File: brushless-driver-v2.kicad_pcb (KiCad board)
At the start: 2 copper layers, 86.5 x 63 mm, 52 parts, among them J1 Conn_01x07_Socket, J2 encoder, J3 motor, U1 TCMT1100, U2 TCMT1100, U3 TCMT1100, U5 L7805

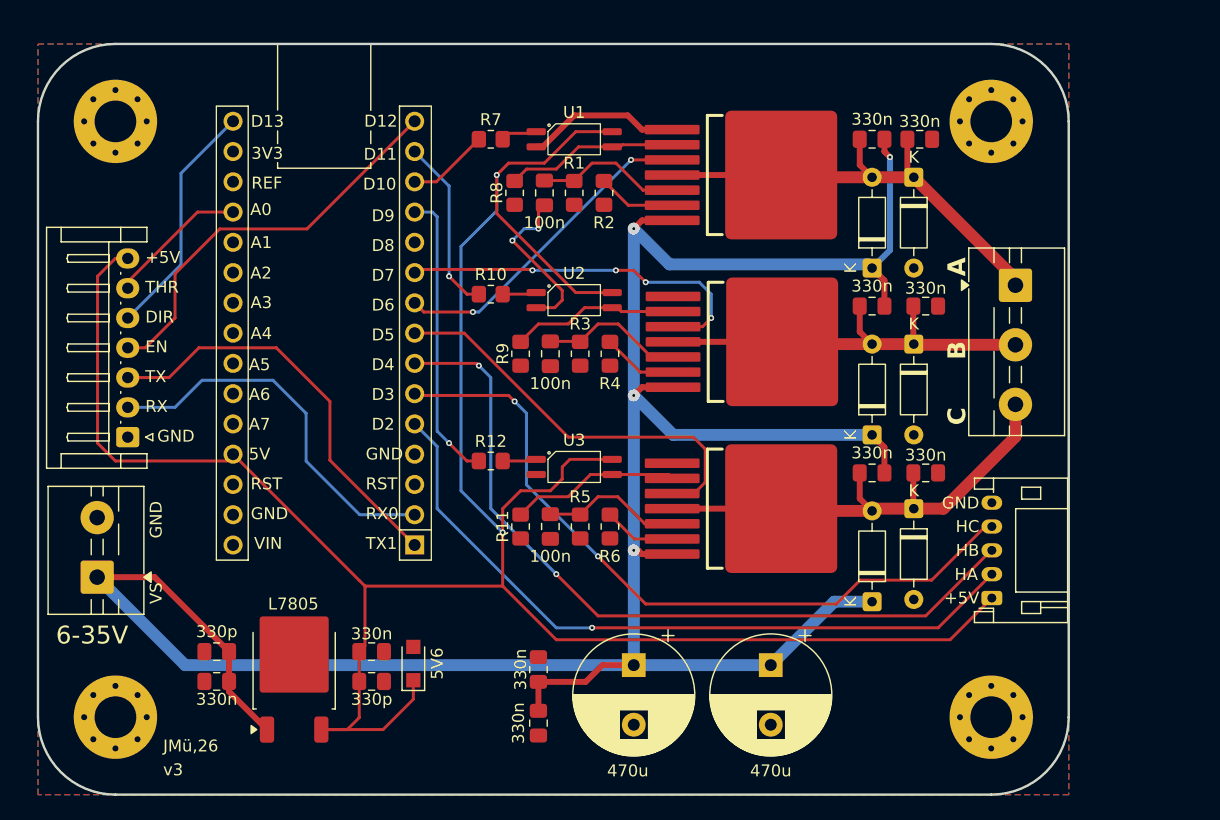
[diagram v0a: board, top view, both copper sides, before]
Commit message: Updated Footprint of JST connector to 2mm pitch
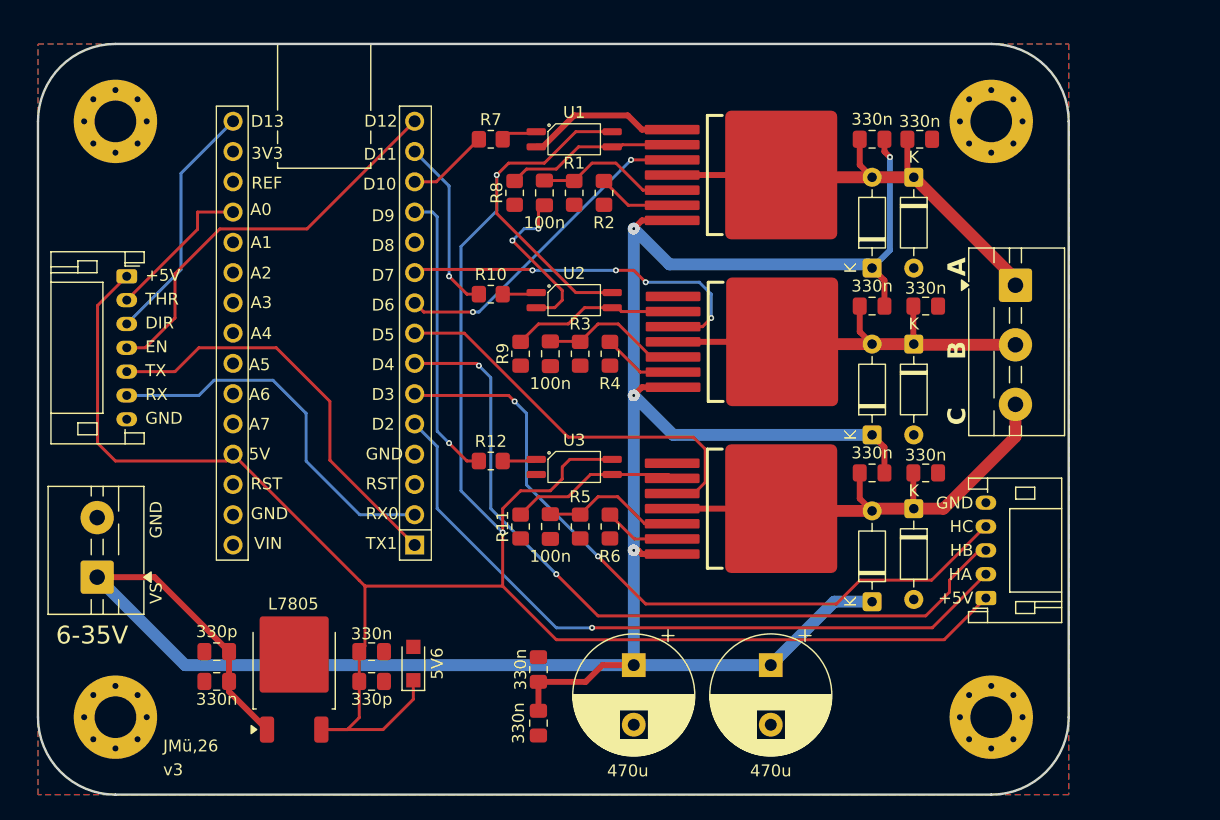
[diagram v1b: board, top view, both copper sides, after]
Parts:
- J1: footprint Connector_JST:JST_EH_S7B-EH_1x07_P2.50mm_Horizontal -> Connector_JST:JST_PH_S7B-PH-K_1x07_P2.00mm_Horizontal
- moved J1 13.5 mm to (111.0, 103.0), turned to -90 degrees
- moved J2 0.50 mm to (183.1, 130.0)
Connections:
- J1 pad 1: GND -> +5V
- J1 pad 2: RX -> THR
- J1 pad 3: TX -> DIR
- J1 pad 5: DIR -> TX
- J1 pad 6: THR -> RX
- J1 pad 7: +5V -> GND
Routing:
- net +5V: track 203.7 -> 201.1 mm
- net THR: track 11.8 -> 12.8 mm
- net HC: track 62.0 -> 61.4 mm
- net DIR: track 20.2 -> 20.7 mm
- net HA: track 60.4 -> 59.9 mm

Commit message: Improvements, more to be done
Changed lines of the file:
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@@
 		)
 		(fp_text user "K"
-			(at -1.5 0 180)
+			(at -1.5 0 0)
 			(layer "F.SilkS")
 			(effects
@@
 			(at 0 -1.68 90)
 			(layer "F.SilkS")
-			(hide yes)
 			(effects
 				(font
@@
 			(at 7.367677 -4 0)
 			(layer "F.SilkS")
-			(hide yes)
 			(effects
 				(font
@@
 			(at 0 -1.68 0)
 			(layer "F.SilkS")
-			(hide yes)
 			(effects
 				(font
@@
 			(at 0 -1.68 0)
 			(layer "F.SilkS")
-			(hide yes)
 			(effects
 				(font
@@
 			(at 0 -3.575 90)
 			(layer "F.SilkS")
-			(hide yes)
 			(effects
 				(font
@@
 			(at 0 -4.45 0)
 			(layer "F.SilkS")
-			(hide yes)
 			(effects
 				(font
@@
 			(at 3.81 -2.12 90)
 			(layer "F.SilkS")
-			(hide yes)
 			(effects
 				(font
@@
 			(at 0 -1.68 0)
 			(layer "F.SilkS")
-			(hide yes)
 			(effects
 				(font
@@
 			(at 0 -1.68 0)
 			(layer "F.SilkS")
-			(hide yes)
 			(effects
 				(font
@@
 		)
 		(fp_text user "K"
-			(at -1.69 0 180)
+			(at -1.69 0 0)
 			(layer "F.SilkS")
 			(effects
@@
 			(at 0 -1.68 0)
 			(layer "F.SilkS")
-			(hide yes)
 			(effects
 				(font
@@
 			(at 0 -4.45 0)
 			(layer "F.SilkS")
-			(hide yes)
 			(effects
 				(font
@@
 			(at 6 -2.55 90)
 			(layer "F.SilkS")
-			(hide yes)
 			(effects
 				(font
@@
 			(at 0 -1.68 0)
 			(layer "F.SilkS")
-			(hide yes)
 			(effects
 				(font
@@
 			(at 0 -1.68 0)
 			(layer "F.SilkS")
-			(hide yes)
 			(effects
 				(font
@@
 			(at 0 -3.5 90)
 			(layer "F.SilkS")
-			(hide yes)
 			(effects
 				(font
@@
 			(at 2.25 -5.12 90)
 			(layer "F.SilkS")
-			(hide yes)
 			(effects
 				(font
@@
 			(at 0 -1.68 90)
 			(layer "F.SilkS")
-			(hide yes)
 			(effects
 				(font
@@
 		)
 		(fp_text user "K"
-			(at -1.69 0 180)
+			(at -1.69 0 0)
 			(layer "F.SilkS")
 			(effects
@@
 			(at 0 -1.68 90)
 			(layer "F.SilkS")
-			(hide yes)
 			(effects
 				(font
@@
 			(at 0 -4.45 0)
 			(layer "F.SilkS")
-			(hide yes)
 			(effects
 				(font
@@
 			(at 0 -4.5 90)
 			(layer "F.SilkS")
-			(hide yes)
 			(effects
 				(font
@@
 			(at 7.367677 -5.5 0)
 			(layer "F.SilkS")
-			(hide yes)
 			(effects
 				(font
@@
 			(at 7.62 -5.08 180)
 			(layer "F.SilkS")
-			(hide yes)
 			(effects
 				(font
@@
 			(at 0 -2 90)
 			(layer "F.SilkS")
-			(hide yes)
 			(effects
 				(font
@@
 			(at 0 -1.68 0)
 			(layer "F.SilkS")
-			(hide yes)
 			(effects
 				(font
@@
 			(at 0 -3.5 90)
 			(layer "F.SilkS")
-			(hide yes)
 			(effects
 				(font
@@
 			(at 0 -1.68 90)
 			(layer "F.SilkS")
-			(hide yes)
 			(effects
 				(font
@@
 		(tags "THT terminal block MaiXu MX126-5.0-03P pitch 5mm size 15.5x7.8mm drill 1.3mm pad 2.8mm")
 		(property "Reference" "J3"
-			(at 4.75 -5.12 270)
+			(at 4.75 -5.12 90)
 			(layer "F.SilkS")
 			(hide yes)
@@
 		)
 		(property "Value" "motor"
-			(at 4.75 4.92 270)
+			(at 4.75 4.92 90)
 			(layer "F.Fab")
 			(hide yes)
@@
 		)
 		(property "Datasheet" "~"
-			(at 0 0 270)
+			(at 0 0 90)
 			(layer "F.Fab")
 			(hide yes)
@@
 		)
 		(property "Description" ""
-			(at 0 0 270)
+			(at 0 0 90)
 			(layer "F.Fab")
 			(hide yes)
@@
 		)
 		(fp_text user "${REFERENCE}"
-			(at 4.75 2.65 270)
+			(at 4.75 2.65 90)
 			(layer "F.Fab")
 			(effects
@@
 			(at 0 -4.45 0)
 			(layer "F.SilkS")
-			(hide yes)
 			(effects
 				(font
@@
 			(at 3.81 -2.12 90)
 			(layer "F.SilkS")
-			(hide yes)
 			(effects
 				(font
@@
 			(at 0 -1.68 90)
 			(layer "F.SilkS")
-			(hide yes)
 			(effects
 				(font
@@
 			(at 0 -1.68 0)
 			(layer "F.SilkS")
-			(hide yes)
 			(effects
 				(font
@@
 			(at 0 -1.68 0)
 			(layer "F.SilkS")
-			(hide yes)
 			(effects
 				(font
@@
 	)
 	(gr_text "+5V"
-		(at 182 130 0)
+		(at 181.5 130 0)
 		(layer "F.SilkS")
 		(effects
@@
 	)
 	(gr_text "A"
-		(at 181.5 103 90)
+		(at 180.5 103 90)
 		(layer "F.SilkS")
 		(effects
@@
 	)
 	(gr_text "GND"
-		(at 114 125 90)
+		(at 116.5 125 90)
 		(layer "F.SilkS")
 		(effects
@@
 	)
 	(gr_text "HC"
-		(at 182 124 0)
+		(at 181.5 124 0)
 		(layer "F.SilkS")
 		(effects
@@
 	)
 	(gr_text "B"
-		(at 181.5 110 90)
+		(at 180.5 110 90)
 		(layer "F.SilkS")
 		(effects
@@
 	)
 	(gr_text "HB"
-		(at 182 126 0)
+		(at 181.5 126 0)
 		(layer "F.SilkS")
 		(effects
@@
 	)
 	(gr_text "VS"
-		(at 114 130.5 90)
+		(at 116.5 130.5 90)
 		(layer "F.SilkS")
 		(effects
@@
 	)
 	(gr_text "GND"
-		(at 182.001112 122.023428 0)
+		(at 181.501112 122.023428 0)
 		(layer "F.SilkS")
 		(effects
@@
 	)
 	(gr_text "C"
-		(at 181.5 115.5 90)
+		(at 180.5 115.5 90)
 		(layer "F.SilkS")
 		(effects
@@
 	)
 	(gr_text "HA"
-		(at 181.887958 128.020615 0)
+		(at 181.387958 128.020615 0)
 		(layer "F.SilkS")
 		(effects

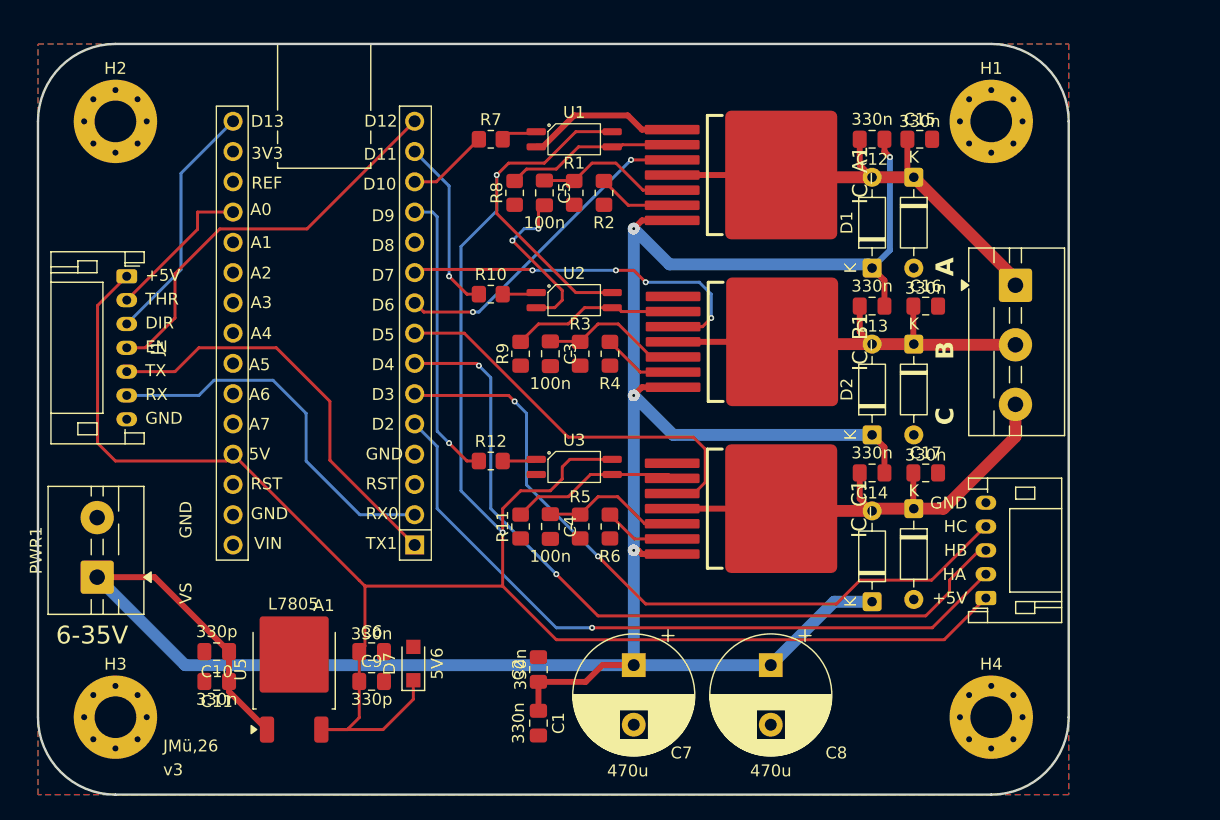
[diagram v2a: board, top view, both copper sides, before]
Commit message: Started on version 3. Major redesign according to dev board for the IFX007T. Previous version was unfit for continous operation - now zones instead of traces for high current lines.
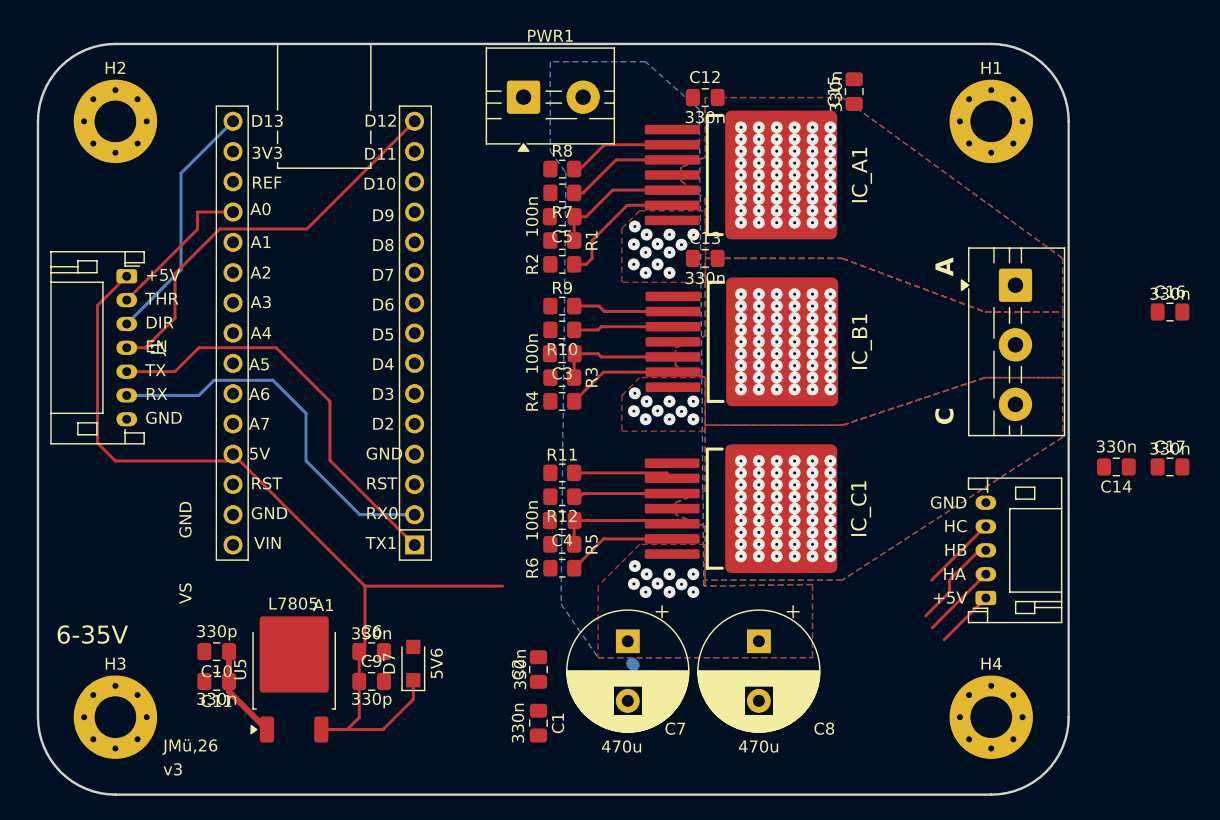
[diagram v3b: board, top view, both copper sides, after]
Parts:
- removed D1, D2, D3, D4, D5, D6: 1N914, Diode_THT:D_DO-35_SOD27_P7.62mm_Horizontal
- removed U1, U2, U3: TCMT1100, meiBib:SOP-4_4.4x2.6mm_P1.27mm
- R10, R12, R7: value 220R -> 10k
- moved PWR1 53.9 mm to (144.2, 88.0), turned to 0 degrees
- moved C14 20.5 mm to (194.0, 119.0)
- moved C16 20.5 mm to (198.5, 106.0)
- moved C17 20.5 mm to (198.5, 119.0)
- moved C13 14.6 mm to (159.5, 101.5), turned to 0 degrees
- moved C12 14.4 mm to (159.5, 88.0), turned to 0 degrees
- moved R7 7.50 mm to (147.5, 96.0), turned to 180 degrees
- moved R2 6.95 mm to (147.5, 102.0), turned to 180 degrees
- moved C15 6.80 mm to (172.0, 87.5), turned to 90 degrees
- moved R10 6.71 mm to (147.5, 107.5), turned to 180 degrees
- moved R12 6.71 mm to (147.5, 121.5), turned to 180 degrees
- moved R11 5.70 mm to (147.5, 119.5), turned to 180 degrees
- moved R4 5.66 mm to (147.5, 113.5), turned to 180 degrees
- moved R6 5.32 mm to (147.5, 127.5), turned to 180 degrees
- moved R9 5.32 mm to (147.5, 105.5), turned to 180 degrees
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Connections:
- net Net-(D1-A) renamed A_OUT
- net Net-(D2-A) renamed B_OUT
- net Net-(D3-A) renamed C_OUT
- IC_A1 pad 3: INH_A -> Net-(IC_A1-INH)
- IC_B1 pad 3: INH_B -> Net-(IC_B1-INH)
- IC_C1 pad 3: INH_C -> Net-(IC_C1-INH)
- PWR1 pad 1: VS -> GND
- PWR1 pad 2: GND -> VS
- R10 pad 1: B -> Net-(IC_B1-INH)
- R10 pad 2: Net-(R10-Pad2) -> INH_B
- R11 pad 2: GND -> C
- R12 pad 1: C -> Net-(IC_C1-INH)
- R12 pad 2: Net-(R12-Pad2) -> INH_C
- R7 pad 1: A -> Net-(IC_A1-INH)
- R7 pad 2: Net-(R7-Pad2) -> INH_A
- R8 pad 2: GND -> A
- R9 pad 2: GND -> B
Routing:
- net VS: track 212.2 -> 8.51 mm, vias 4 -> 33
- net +5V: track 201.1 -> 84.6 mm, vias 2 -> 0
- net HB: track 66.0 -> 7.91 mm, vias 2 -> 0
- net HC: track 61.4 -> 6.58 mm, vias 2 -> 0
- net HA: track 59.9 -> 6.36 mm, vias 1 -> 0
- net C_OUT: track 41.0 -> 0.27 mm, vias 0 -> 54
- net A_OUT: track 40.0 -> 0.80 mm, vias 0 -> 54
- net B_OUT: track 35.7 -> 0.27 mm, vias 0 -> 54
- net INH_C: track 34.4 -> 0.00 mm
- net INH_B: track 31.4 -> 0.38 mm, vias 4 -> 0
- net INH_A: track 27.2 -> 0.00 mm, vias 2 -> 0
- net GND: track 27.0 -> 0.00 mm, vias 2 -> 0
- net C: track 24.6 -> 0.00 mm, vias 1 -> 0
- net B: track 14.8 -> 0.00 mm, vias 1 -> 0
- net Net-(IC_A1-INH): track 0.00 -> 9.37 mm
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- added copper zone on B.Cu, net A_OUT
- added copper zone on F.Cu, net A_OUT
- added copper zone on B.Cu, net B_OUT
- added copper zone on F.Cu, net B_OUT
- added copper zone on B.Cu, net C_OUT
- added copper zone on F.Cu, net C_OUT
- added copper zone on B.Cu, net VS
- added copper zone on F.Cu, net VS
- removed copper zone on B.Cu, net GND
- removed copper zone on F.Cu, net GND
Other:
- board text removed: "B"

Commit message: finished rework
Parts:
- removed C12, C13, C14, C15, C16, C17: 330n, Capacitor_SMD:C_0805_2012Metric_Pad1.18x1.45mm_HandSolder
- R1, R3, R5: value 10k -> 5k6
- moved C1 7.02 mm to (146.0, 133.5), turned to 180 degrees
- moved C2 5.52 mm to (146.0, 130.5), turned to 180 degrees
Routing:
- net HC: track 6.58 -> 80.5 mm, vias 0 -> 1
- net HB: track 7.91 -> 80.6 mm
- net HA: track 6.36 -> 76.7 mm
- net +5V: track 84.6 -> 125.0 mm
- net VS: track 8.51 -> 43.9 mm, vias 33 -> 49
- net C: track 0.00 -> 31.9 mm, vias 0 -> 1
- net INH_C: track 0.00 -> 23.5 mm, vias 0 -> 1
- net B: track 0.00 -> 23.2 mm, vias 0 -> 1
- net INH_A: track 0.00 -> 19.3 mm
- net INH_B: track 0.38 -> 15.5 mm, vias 0 -> 1
- net A: track 0.00 -> 11.8 mm, vias 0 -> 1
- net THR: track 12.8 -> 12.0 mm
- added copper zone on B.Cu, net GND
- added copper zone on F.Cu, net GND
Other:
- board text added: "B"
- board text added: "v4"
- board text removed: "v3"

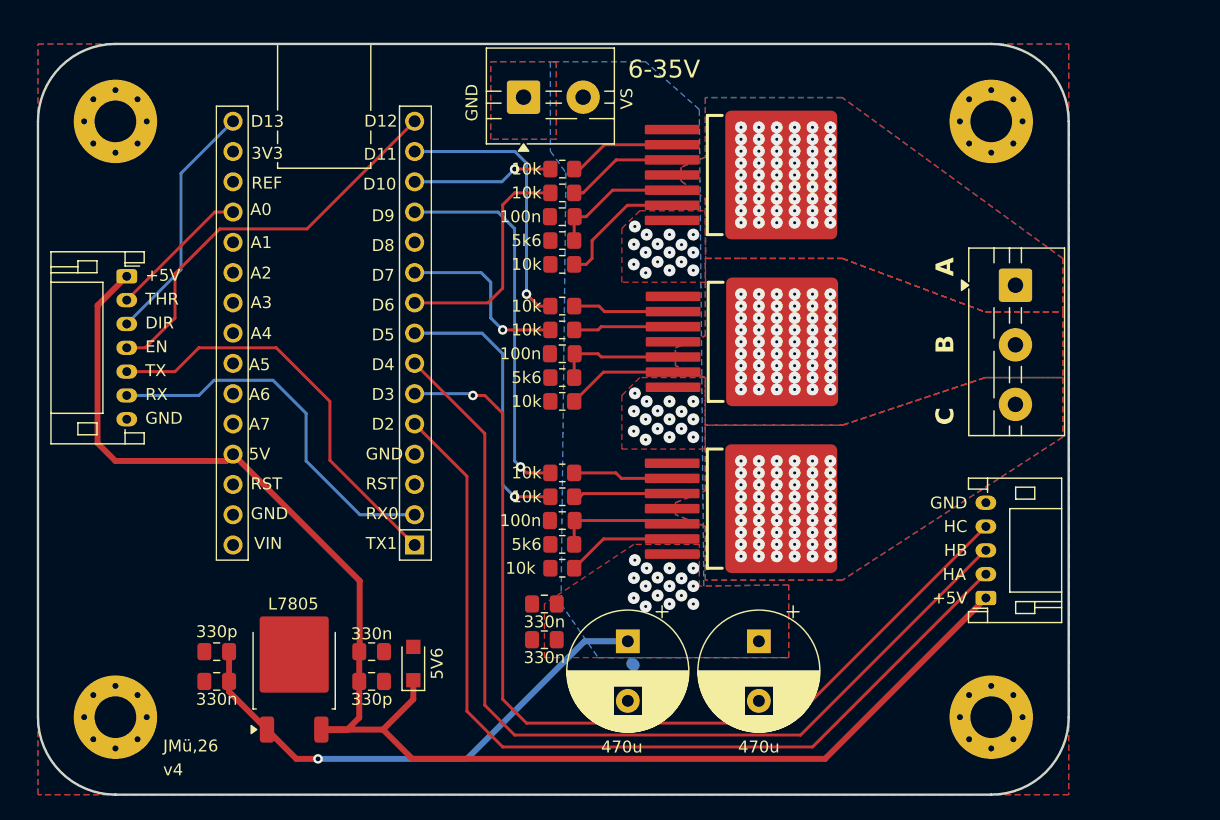
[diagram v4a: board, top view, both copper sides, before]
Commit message: Improvements to routing of power signals
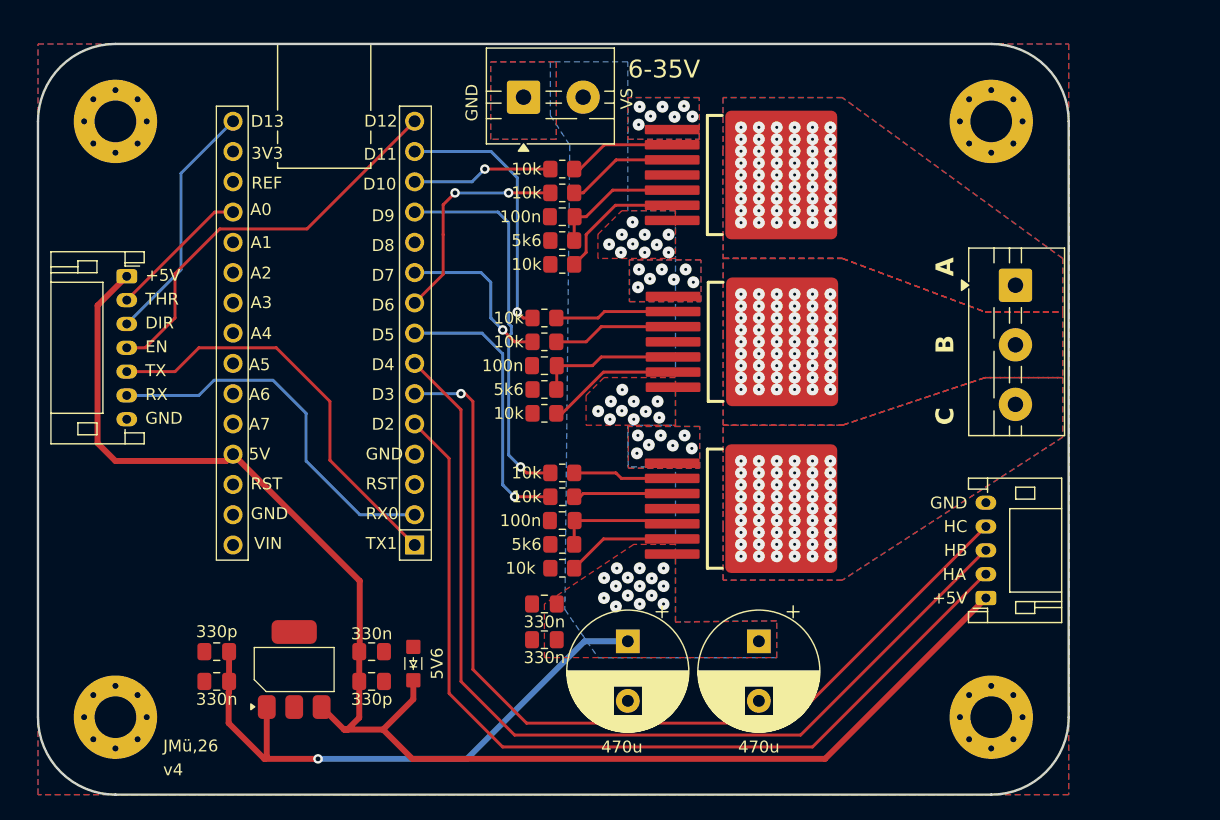
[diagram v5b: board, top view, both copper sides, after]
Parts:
- D7: footprint Diode_SMD:Nexperia_CFP3_SOD-123W -> meiBib:SOD-123W
- U5: footprint Package_TO_SOT_SMD:TO-252-2 -> meiBib:SOT-223-3_TabPin2
- moved C3 1.80 mm to (146.0, 110.5)
- moved R10 1.80 mm to (146.0, 108.5)
- moved R3 1.80 mm to (146.0, 112.5)
- moved R4 1.80 mm to (146.0, 114.5)
- moved R9 1.80 mm to (146.0, 106.5)
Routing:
- net VS: track 43.9 -> 49.7 mm, vias 49 -> 36
- net Net-(IC_B1-INH): track 8.41 -> 10.3 mm
- net Net-(IC_B1-IS): track 9.32 -> 11.2 mm
- net Net-(IC_B1-SR): track 10.4 -> 12.1 mm
- net Net-(IC_B1-IN): track 8.49 -> 10.0 mm
- net +5V: track 125.0 -> 123.8 mm
- net INH_B: track 15.5 -> 14.4 mm
- net B: track 23.2 -> 22.3 mm
- net HC: track 80.5 -> 79.6 mm
- net INH_A: track 19.3 -> 18.6 mm, vias 0 -> 2
- net GND: vias 0 -> 21
